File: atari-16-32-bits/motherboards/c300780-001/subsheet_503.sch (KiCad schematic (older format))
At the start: 39 parts, among them Q500 LM78L82_TO92, U504 LF347N_mu, U505 MF4CN-100_PHY, U506 MF4CN-100_PHY, U507 LF347N_mu

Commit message: Fixes #51 : [bug][schematics] fix the association of mlcc capacitors and their footprint in schematics to match the association done in the pcb
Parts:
- C500, C501, C502, C511, C512, C513, C514, C523, C565: footprint commons_passives_THT:Passive_THT_capacitor_ceramic_radial_W5.08mm_L6.35mm_X11.43mm -> commons_passives_THT:Passive_THT_capacitor_mlcc_W2.54mm_L7.62mm
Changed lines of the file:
@@
 F 0 "C501" H 1625 8400 50  0000 L CNN
 F 1 "0.1uF" H 1625 8200 50  0000 L CNN
-F 2 "commons_passives_THT:Passive_THT_capacitor_ceramic_radial_W5.08mm_L6.35mm_X11.43mm" H 1638 8150 50  0001 C CNN
+F 2 "commons_passives_THT:Passive_THT_capacitor_mlcc_W2.54mm_L7.62mm" H 1638 8150 50  0001 C CNN
 F 3 "~" H 1600 8300 50  0001 C CNN
 	1    1600 8300
@@
 F 0 "C512" H 1625 9000 50  0000 L CNN
 F 1 "0.1uF" H 1625 8800 50  0000 L CNN
-F 2 "commons_passives_THT:Passive_THT_capacitor_ceramic_radial_W5.08mm_L6.35mm_X11.43mm" H 1638 8750 50  0001 C CNN
+F 2 "commons_passives_THT:Passive_THT_capacitor_mlcc_W2.54mm_L7.62mm" H 1638 8750 50  0001 C CNN
 F 3 "~" H 1600 8900 50  0001 C CNN
 	1    1600 8900
@@
 F 0 "C500" H 875 8400 50  0000 L CNN
 F 1 "0.1uF" H 875 8200 50  0000 L CNN
-F 2 "commons_passives_THT:Passive_THT_capacitor_ceramic_radial_W5.08mm_L6.35mm_X11.43mm" H 888 8150 50  0001 C CNN
+F 2 "commons_passives_THT:Passive_THT_capacitor_mlcc_W2.54mm_L7.62mm" H 888 8150 50  0001 C CNN
 F 3 "~" H 850 8300 50  0001 C CNN
 	1    850  8300
@@
 F 0 "C511" H 875 9000 50  0000 L CNN
 F 1 "0.1uF" H 875 8800 50  0000 L CNN
-F 2 "commons_passives_THT:Passive_THT_capacitor_ceramic_radial_W5.08mm_L6.35mm_X11.43mm" H 888 8750 50  0001 C CNN
+F 2 "commons_passives_THT:Passive_THT_capacitor_mlcc_W2.54mm_L7.62mm" H 888 8750 50  0001 C CNN
 F 3 "~" H 850 8900 50  0001 C CNN
 	1    850  8900
@@
 F 0 "C502" H 3125 8400 50  0000 L CNN
 F 1 "0.1uF" H 3125 8200 50  0000 L CNN
-F 2 "commons_passives_THT:Passive_THT_capacitor_ceramic_radial_W5.08mm_L6.35mm_X11.43mm" H 3138 8150 50  0001 C CNN
+F 2 "commons_passives_THT:Passive_THT_capacitor_mlcc_W2.54mm_L7.62mm" H 3138 8150 50  0001 C CNN
 F 3 "~" H 3100 8300 50  0001 C CNN
 	1    3100 8300
@@
 F 0 "C513" H 3125 9000 50  0000 L CNN
 F 1 "0.1uF" H 3125 8800 50  0000 L CNN
-F 2 "commons_passives_THT:Passive_THT_capacitor_ceramic_radial_W5.08mm_L6.35mm_X11.43mm" H 3138 8750 50  0001 C CNN
+F 2 "commons_passives_THT:Passive_THT_capacitor_mlcc_W2.54mm_L7.62mm" H 3138 8750 50  0001 C CNN
 F 3 "~" H 3100 8900 50  0001 C CNN
 	1    3100 8900
@@
 F 0 "C514" H 2375 8400 50  0000 L CNN
 F 1 "0.1uF" H 2375 8200 50  0000 L CNN
-F 2 "commons_passives_THT:Passive_THT_capacitor_ceramic_radial_W5.08mm_L6.35mm_X11.43mm" H 2388 8150 50  0001 C CNN
+F 2 "commons_passives_THT:Passive_THT_capacitor_mlcc_W2.54mm_L7.62mm" H 2388 8150 50  0001 C CNN
 F 3 "~" H 2350 8300 50  0001 C CNN
 	1    2350 8300
@@
 F 0 "C523" H 2375 9000 50  0000 L CNN
 F 1 "0.1uF" H 2375 8800 50  0000 L CNN
-F 2 "commons_passives_THT:Passive_THT_capacitor_ceramic_radial_W5.08mm_L6.35mm_X11.43mm" H 2388 8750 50  0001 C CNN
+F 2 "commons_passives_THT:Passive_THT_capacitor_mlcc_W2.54mm_L7.62mm" H 2388 8750 50  0001 C CNN
 F 3 "~" H 2350 8900 50  0001 C CNN
 	1    2350 8900
@@
 F 0 "C565" H 6875 1150 50  0000 L CNN
 F 1 "0.1uF" H 6875 950 50  0000 L CNN
-F 2 "commons_passives_THT:Passive_THT_capacitor_ceramic_radial_W5.08mm_L6.35mm_X11.43mm" H 6888 900 50  0001 C CNN
+F 2 "commons_passives_THT:Passive_THT_capacitor_mlcc_W2.54mm_L7.62mm" H 6888 900 50  0001 C CNN
 F 3 "~" H 6850 1050 50  0001 C CNN
 	1    6850 1050

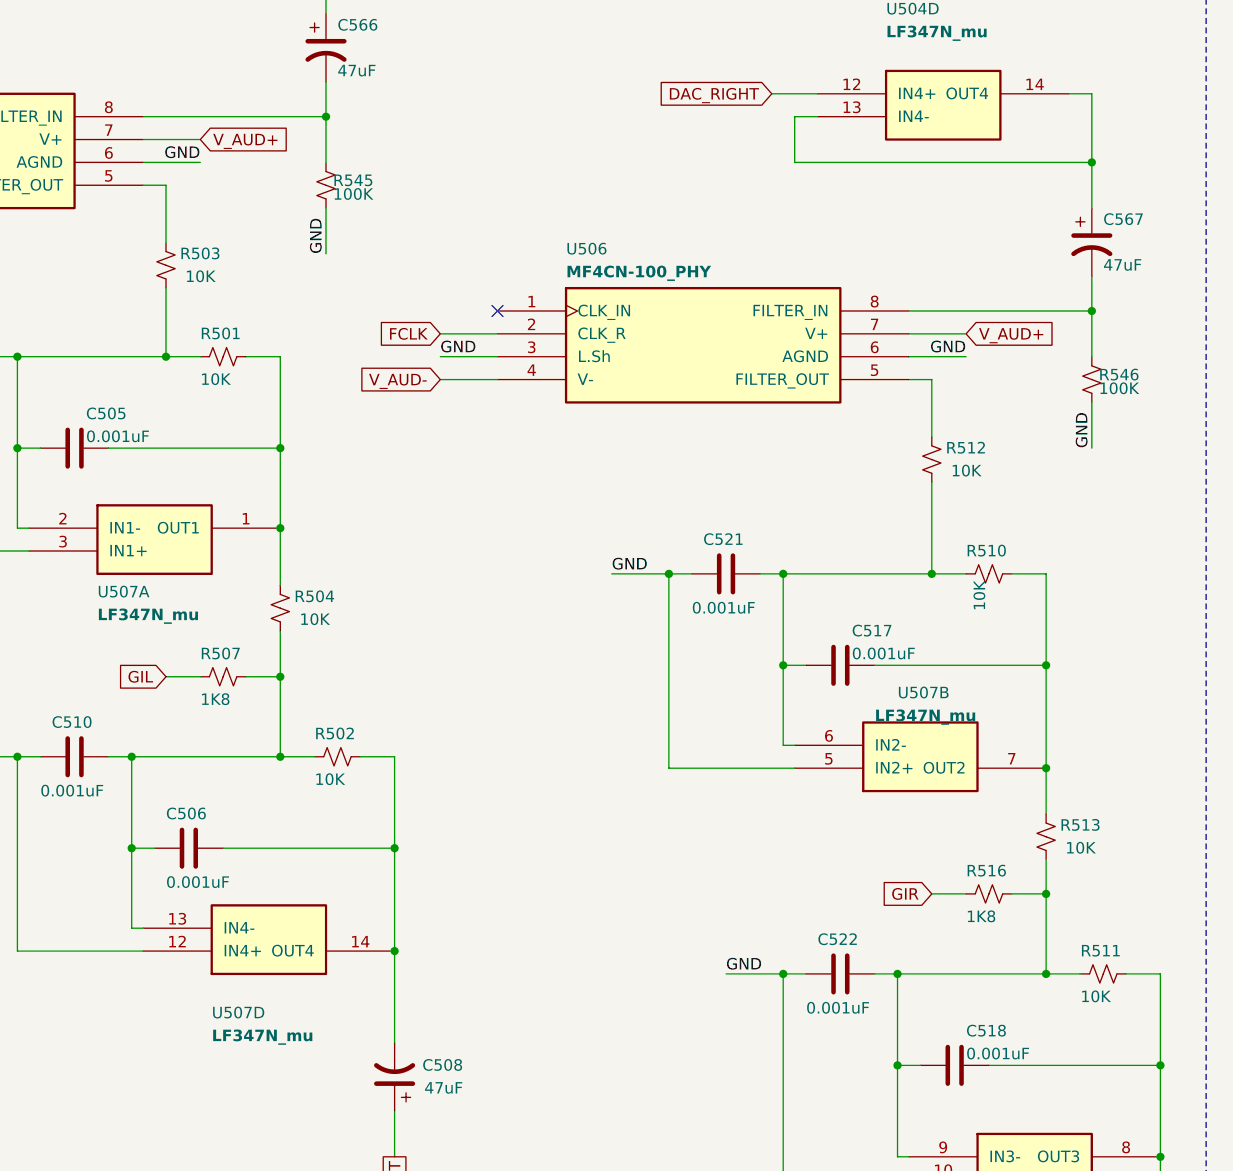
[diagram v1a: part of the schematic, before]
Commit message: [BOM] add '1%' marker on resistors values for the dac/audio amp
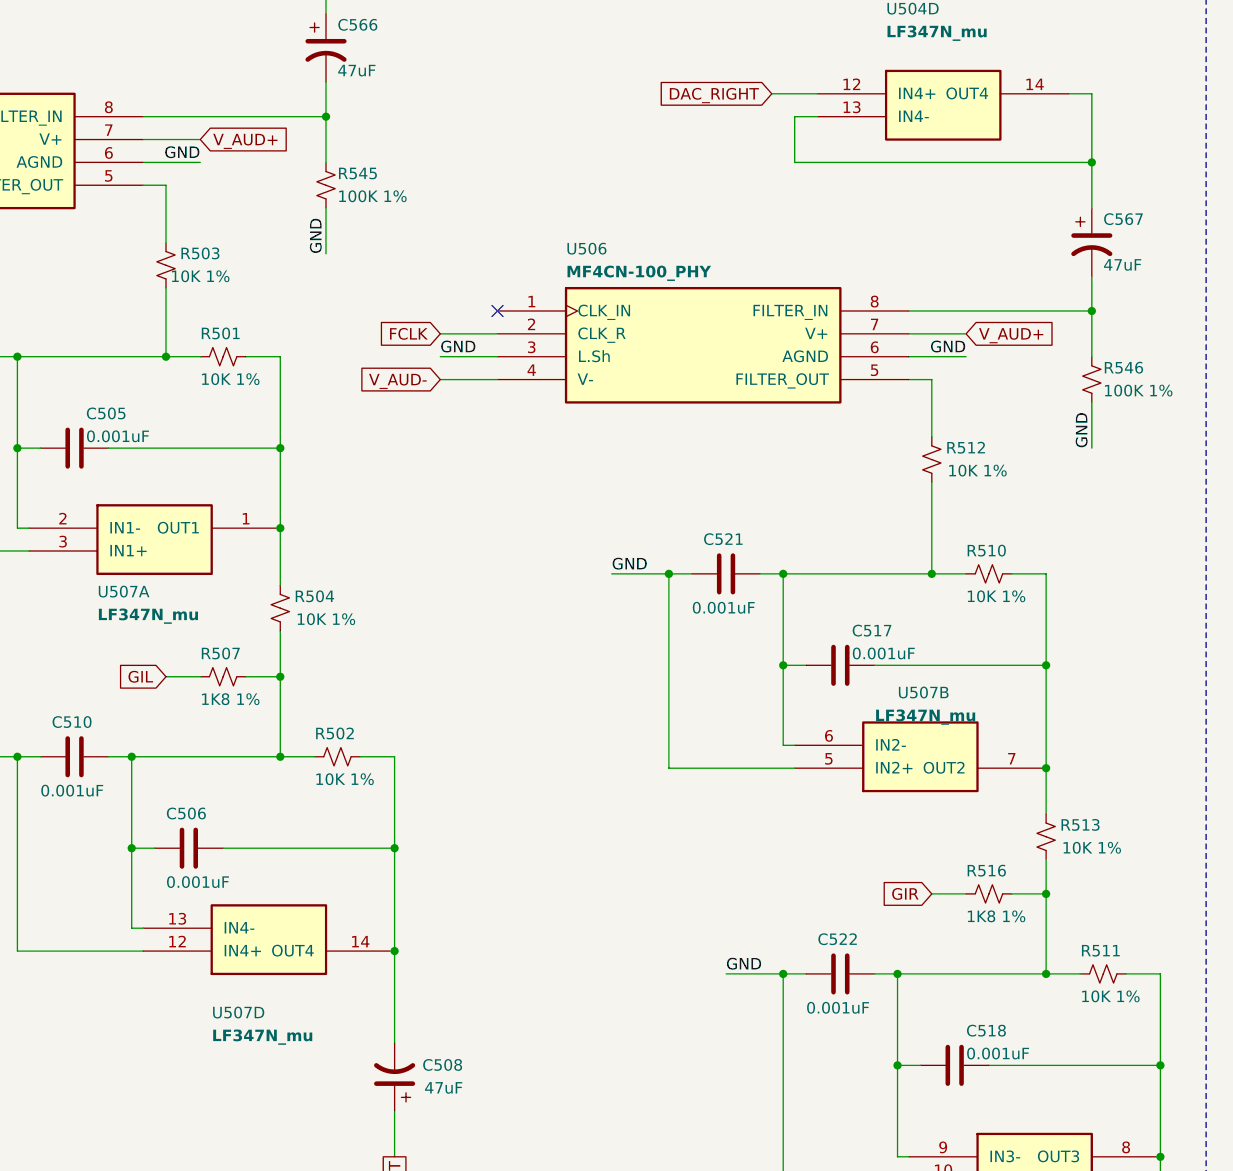
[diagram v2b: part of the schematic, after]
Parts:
- R501, R502, R503, R504, R510, R511, R512, R513: value 10K -> 10K 1%
- R507, R516: value 1K8 -> 1K8 1%
- R545, R546: value 100K -> 100K 1%
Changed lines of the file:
@@
 AR Path="/60C95DE8/60D196CE" Ref="R?"  Part="1"
 AR Path="/60CC3B10/60D196CE" Ref="R545"  Part="1"
-F 0 "R545" H 3880 2570 50  0000 L CNN
-F 1 "100K" H 3880 2510 50  0000 L CNN
+F 0 "R545" H 3900 2600 50  0000 L CNN
+F 1 "100K 1%" H 3900 2500 50  0000 L CNN
 F 2 "commons_passives_THT:Passive_THT_resistor_W2.54mm_L12.70mm" H 3850 2550 50  0001 C CNN
 F 3 "~" H 3850 2550 50  0001 C CNN
@@
 AR Path="/60C95DE8/60DEF293" Ref="R?"  Part="1"
 AR Path="/60CC3B10/60DEF293" Ref="R546"  Part="1"
-F 0 "R546" H 7230 3420 50  0000 L CNN
-F 1 "100K" H 7230 3360 50  0000 L CNN
+F 0 "R546" H 7250 3450 50  0000 L CNN
+F 1 "100K 1%" H 7250 3350 50  0000 L CNN
 F 2 "commons_passives_THT:Passive_THT_resistor_W2.54mm_L12.70mm" H 7200 3400 50  0001 C CNN
 F 3 "~" H 7200 3400 50  0001 C CNN
@@
 AR Path="/60CC3B10/60E9CB1B" Ref="R513"  Part="1"
 F 0 "R513" H 6850 5350 50  0000 C CNN
-F 1 "10K" H 6850 5450 50  0000 C CNN
+F 1 "10K 1%" H 6800 5450 50  0000 C CNN
 F 2 "commons_passives_THT:Passive_THT_resistor_W2.54mm_L12.70mm" H 7000 5400 50  0001 C CNN
 F 3 "~" H 7000 5400 50  0001 C CNN
@@
 AR Path="/60CC3B10/60E9CB27" Ref="R511"  Part="1"
 F 0 "R511" V 7150 5900 50  0000 L CNN
-F 1 "10K" V 7350 5900 50  0000 L CNN
+F 1 "10K 1%" V 7350 5900 50  0000 L CNN
 F 2 "commons_passives_THT:Passive_THT_resistor_W2.54mm_L12.70mm" H 7250 6000 50  0001 C CNN
 F 3 "~" H 7250 6000 50  0001 C CNN
@@
 AR Path="/60CC3B10/60E9CB37" Ref="R512"  Part="1"
 F 0 "R512" H 6350 3700 50  0000 C CNN
-F 1 "10K" H 6350 3800 50  0000 C CNN
+F 1 "10K 1%" H 6300 3800 50  0000 C CNN
 F 2 "commons_passives_THT:Passive_THT_resistor_W2.54mm_L12.70mm" H 6500 3750 50  0001 C CNN
 F 3 "~" H 6500 3750 50  0001 C CNN
@@
 AR Path="/60CC3B10/60E9CB43" Ref="R510"  Part="1"
 F 0 "R510" V 6650 4150 50  0000 L CNN
-F 1 "10K" H 6780 4210 50  0000 L CNN
+F 1 "10K 1%" V 6850 4150 50  0000 L CNN
 F 2 "commons_passives_THT:Passive_THT_resistor_W2.54mm_L12.70mm" H 6750 4250 50  0001 C CNN
 F 3 "~" H 6750 4250 50  0001 C CNN
@@
 AR Path="/60CC3B10/60D0058C" Ref="R516"  Part="1"
 F 0 "R516" V 6650 5550 50  0000 L CNN
-F 1 "1K8" V 6850 5550 50  0000 L CNN
+F 1 "1K8 1%" V 6850 5550 50  0000 L CNN
 F 2 "commons_passives_THT:Passive_THT_resistor_W2.54mm_L12.70mm" H 6750 5650 50  0001 C CNN
 F 3 "~" H 6750 5650 50  0001 C CNN
@@
 AR Path="/60CC3B10/60E9CABA" Ref="R504"  Part="1"
 F 0 "R504" H 3500 4350 50  0000 C CNN
-F 1 "10K" H 3500 4450 50  0000 C CNN
+F 1 "10K 1%" H 3450 4450 50  0000 C CNN
 F 2 "commons_passives_THT:Passive_THT_resistor_W2.54mm_L12.70mm" H 3650 4400 50  0001 C CNN
 F 3 "~" H 3650 4400 50  0001 C CNN
@@
 AR Path="/60CC3B10/60E9CAC6" Ref="R502"  Part="1"
 F 0 "R502" V 3800 4950 50  0000 L CNN
-F 1 "10K" V 4000 4950 50  0000 L CNN
+F 1 "10K 1%" V 4000 4950 50  0000 L CNN
 F 2 "commons_passives_THT:Passive_THT_resistor_W2.54mm_L12.70mm" H 3900 5050 50  0001 C CNN
 F 3 "~" H 3900 5050 50  0001 C CNN
@@
 AR Path="/60CC3B10/60E9CAD6" Ref="R503"  Part="1"
 F 0 "R503" H 3000 2850 50  0000 C CNN
-F 1 "10K" H 3000 2950 50  0000 C CNN
+F 1 "10K 1%" H 3000 2950 50  0000 C CNN
 F 2 "commons_passives_THT:Passive_THT_resistor_W2.54mm_L12.70mm" H 3150 2900 50  0001 C CNN
 F 3 "~" H 3150 2900 50  0001 C CNN
@@
 AR Path="/60CC3B10/60E9CAE2" Ref="R501"  Part="1"
 F 0 "R501" V 3300 3200 50  0000 L CNN
-F 1 "10K" V 3500 3200 50  0000 L CNN
+F 1 "10K 1%" V 3500 3200 50  0000 L CNN
 F 2 "commons_passives_THT:Passive_THT_resistor_W2.54mm_L12.70mm" H 3400 3300 50  0001 C CNN
 F 3 "~" H 3400 3300 50  0001 C CNN
@@
 AR Path="/60CC3B10/60CFACA6" Ref="R507"  Part="1"
 F 0 "R507" V 3300 4600 50  0000 L CNN
-F 1 "1K8" V 3500 4600 50  0000 L CNN
+F 1 "1K8 1%" V 3500 4600 50  0000 L CNN
 F 2 "commons_passives_THT:Passive_THT_resistor_W2.54mm_L12.70mm" H 3400 4700 50  0001 C CNN
 F 3 "~" H 3400 4700 50  0001 C CNN
